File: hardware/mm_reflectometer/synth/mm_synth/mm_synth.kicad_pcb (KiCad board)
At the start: 6 copper layers, 680 parts, among them J1001 Conn_Coaxial, J1002 Conn_Coaxial, J1501 1725656, J1502 1053091202, J1601 USB_C_Receptacle_USB2.0, J1603 JTAG, J1604 Flash, J1701 Conn_Coaxial, J1702 Conn_Coaxial, J1801 SYZYGY-STD, J1802 PMOD, J1803 PMOD, J2001 Conn_Coaxial, J2002 Conn_Coaxial, J2003 Conn_Coaxial, J2004 Conn_Coaxial, J2101 USB_C_Receptacle_USB2.0, J301 Conn_Coaxial, J302 Conn_Coaxial, K301 1-1462051-1, Q1101 BC848W, Q1102 IRLML6401, Q1501 FDS6890A, Q1901 BC848W, Q1902 IRLML6401, Q2101 VBZA4435, Q301 IRLML6401, SW1601 SW_Push, SW1602 SW_Push, U1201 TLV9151IDCKR, U1301 LMT86DCK, U1302 TLV9151IDCKR, U1303 AD7298, U1304 VEMI65AB-HCI, U1501 LTM4622A, U1502 LTC4365DDB, U1503 LM3880MF-1AF, U1504 TLV70025_SOT353, U1505 TLV62569DRL, U1506 TLV62569DRL, U1507 TLV70018_SOT353, U1601 ECP5U_25_CABGA256, U1602 93LC56C, U1603 TPD3S014, U1604 FT2232HQ, U1605 W25Q32JVSS, U1701 IS66WVH16M8ALL, U1801 TLV62569DRL, U201 VEMI65AB-HCI, U202 LMX2820, U2101 HUSB238, U301 74AHC1G04, U302 DRV8837C, U303 LTC6957xMS-2, U401 MAAM-011101, U402 ADMV8416, U501 MAAM-011101, U502 XX1000-QT, U503 ADMV8432, U601 ADM7172ACPZ-5.0-R7, U602 LM3880MF-1AF, U603 LM27761, U604 TPS72301DB, U605 TPS72301DB, U606 ADP7158ACPZ-3.3-R7, U607 ADP7158ACPZ-3.3-R7, U608 LT3494, U701 ADRF5042, U702 VEMI65AB-HCI, U703 VEMI65AB-HCI, U704 ADRF5730, U705 MAAM-011109, U706 MAAM-011109, U707 FPC07181, U708 LTC5596, U801 LTC2636IDE-LZ10, U803 TLV9151IDCKR, U804 TLV9151IDCKR, U805 TLV9151IDCKR, U806 TLV9151IDCKR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

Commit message: commit mm_synth prior to updating from june to september kicad-nightly build
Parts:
- removed C631: 1 uF, Capacitor_SMD:C_0402_1005Metric
- added C719: 47 uF, Capacitor_Tantalum_SMD:CP_EIA-3528-15_AVX-H, F.Cu at (225.8, 39.2)
- added C720: 1 uF, Capacitor_SMD:C_0402_1005Metric, F.Cu at (244.8, 42.0)
- added R625: R_Small, Resistor_SMD:R_0402_1005Metric, F.Cu at (196.8, 43.1)
- added R626: R_Small, Resistor_SMD:R_0402_1005Metric, F.Cu at (186.9, 58.7)
- added R627: DNI, Resistor_SMD:R_0402_1005Metric, F.Cu at (183.5, 61.2)
- added R628: DNI, Resistor_SMD:R_0402_1005Metric, F.Cu at (188.8, 52.8)
- C1501, C1526: footprint Capacitor_SMD:CP_Elec_6.3x5.9 -> Capacitor_SMD:CP_Elec_10x12.5
- C1502, C1506: footprint Capacitor_SMD:C_0603_1608Metric -> Capacitor_SMD:C_0805_2012Metric
- C1503, C1509, C1512, C310: value 22 uF -> 10 uF
- C1507, C1508, C647, C648: footprint Capacitor_SMD:C_1210_3225Metric -> Capacitor_Tantalum_SMD:CP_EIA-3528-15_AVX-H
- C227: footprint Capacitor_SMD:C_0603_1608Metric -> Capacitor_SMD:C_1206_3216Metric
- C626, C628: value 1 uF -> DNI
- C630: value 1 uF -> 10 uF; footprint Capacitor_SMD:C_0402_1005Metric -> Capacitor_SMD:C_0805_2012Metric
- C633, C634: value 1 uF -> 1 nF
- U601: value ADM7172ACPZ-5.0-R7 -> ADM7171ACPZ-5.0-R7
- U606, U607: value ADP7158ACPZ-3.3-R7 -> ADM7171ACPZ-R7; footprint Package_DFN_QFN:DFN-10-1EP_3x3mm_P0.5mm_EP1.65x2.38mm -> Package_DFN_QFN:DFN-8-1EP_3x3mm_P0.5mm_EP1.66x2.38mm
- moved C642 152.5 mm to (209.5, 40.0)
- moved R608 151.1 mm to (207.3, 38.1)
- moved R623 147.8 mm to (189.5, 40.6)
- moved C603 146.0 mm to (194.0, 38.3)
- moved C613 145.6 mm to (193.3, 40.8)
- moved R606 145.0 mm to (201.5, 38.1)
- moved R612 144.5 mm to (203.7, 40.0)
- moved R615 143.9 mm to (197.7, 47.1)
- moved C601 143.9 mm to (185.3, 43.0)
- moved FB602 140.7 mm to (187.3, 45.5)
- moved R604 139.2 mm to (190.8, 50.1)
- moved C632 138.2 mm to (203.5, 44.5)
- moved C627 138.0 mm to (196.6, 51.5)
- moved R622 137.6 mm to (202.6, 42.6)
- moved C638 137.1 mm to (179.3, 49.9)
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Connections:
- net /rf_power/15V_BIAS_EN renamed /ctrl_power/DIGITAL_SEQ_EN
- C626 pad 2: GND -> Net-(C626-Pad2)
- C628 pad 2: GND -> Net-(C628-Pad2)
- C630 pad 1: Net-(C630-Pad1) -> +15V
- C636 pad 1: Net-(C636-Pad1) -> Net-(C626-Pad1)
- C637 pad 1: Net-(C637-Pad1) -> Net-(C628-Pad1)
- FB605 pad 1: Net-(C636-Pad1) -> Net-(C626-Pad1)
- FB606 pad 1: Net-(C637-Pad1) -> Net-(C628-Pad1)
- R621 pad 2: Net-(C636-Pad1) -> Net-(C626-Pad1)
- R622 pad 1: Net-(R622-Pad1) -> GND
- R622 pad 2: Net-(C637-Pad1) -> Net-(R621-Pad1)
- U606 pad 1: Net-(C636-Pad1) -> Net-(C626-Pad1)
- U606 pad 2: Net-(C636-Pad1) -> Net-(C626-Pad1)
- U606 pad 4: Net-(C626-Pad1) -> Net-(C633-Pad1)
- U606 pad 6: Net-(C633-Pad1) -> GND
- U606 pad 7: Net-(C633-Pad1) -> +4V
- U606 pad 8: Net-(C630-Pad1) -> +4V
- U606 pad 9: +4V -> GND
- U607 pad 1: Net-(C637-Pad1) -> Net-(C628-Pad1)
- U607 pad 2: Net-(C637-Pad1) -> Net-(C628-Pad1)
- U607 pad 3: Net-(R622-Pad1) -> Net-(R625-Pad1)
- U607 pad 4: Net-(C628-Pad1) -> Net-(C634-Pad1)
- U607 pad 6: Net-(C634-Pad1) -> GND
- U607 pad 7: Net-(C634-Pad1) -> +4V
- U607 pad 8: Net-(C631-Pad1) -> +4V
- U607 pad 9: +4V -> GND
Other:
- copper layers 6 -> 8
- board text added: "0"
- board text added: "0 mm"
- board text added: "0.0000 mm x 0.0000 mm"
- board text added: "0.0037"
- board text added: "0.01 mm"
- board text added: "0.02"
- board text added: "0.035 mm"
- board text added: "0.1 mm"
- board text added: "0.1270 mm / 0.1270 mm"
- board text added: "0.168 mm"
- board text added: "0.2032 mm"
- board text added: "0.35 mm"
- board text added: "1"
- board text added: "1.6360 mm"
- board text added: "3.3"
- board text added: "3.66"
- board text added: "3.7"
- board text added: "4"
- board text added: "8"
- board text added: "B.Cu"
- board text added: "B.Mask"
- board text added: "B.Paste"
- board text added: "B.Silkscreen"
- board text added: "BOARD CHARACTERISTICS"
- board text added: "Board Thickness:"
- board text added: "Board overall dimensions:"
- board text added: "Bottom Silk Screen"
- board text added: "Bottom Solder Mask"
- board text added: "Bottom Solder Paste"
- board text added: "Castellated pads:"
- board text added: "Color"
- board text added: "Copper Finish:"
- board text added: "Copper Layer Count:"
- board text added: "ENIG"
- board text added: "Epsilon R"
- board text added: "F.Cu"
- board text added: "F.Mask"
- board text added: "F.Paste"
- board text added: "F.Silkscreen"
- board text added: "FR4 (IPC 4101/126)"
- board text added: "Green"
- board text added: "Impedance Control:"
- board text added: "In1.Cu"
- board text added: "In2.Cu"
- board text added: "In3.Cu"
- board text added: "In4.Cu"
- board text added: "In5.Cu"
- board text added: "In6.Cu"
- board text added: "Layer Name"
- board text added: "Loss Tangent"
- board text added: "Material"
- board text added: "Min hole diameter:"
- board text added: "Min track/spacing:"
- board text added: "No"
- board text added: "Not specified"
- board text added: "Plated Board Edge:"
- board text added: "RO4350B"
- board text added: "Thickness (mm)"
- board text added: "Top Silk Screen"
- board text added: "Top Solder Mask"
- board text added: "Top Solder Paste"
- board text added: "Type"
- board text added: "White"
- board text added: "Yes"
- board text added: "copper"
- board text added: "core"
- board text added: "prepreg"

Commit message: component placement on mm synth
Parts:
- D1501: value RED -> PMEG030V050EPD; footprint LED_SMD:LED_0603_1608Metric -> Package_TO_SOT_SMD:Nexperia_CFP15_SOT-1289
- D1503: value PMEG030V050EPD -> RED; footprint Package_TO_SOT_SMD:Nexperia_CFP15_SOT-1289 -> LED_SMD:LED_0603_1608Metric
- moved L1502 364.9 mm to (402.8, 146.2)
- moved C1524 356.3 mm to (413.3, 168.0)
- moved C1525 356.0 mm to (413.3, 169.5)
- moved C1516 354.7 mm to (413.7, 174.0)
- moved C1517 353.5 mm to (413.7, 175.5)
- moved C1523 348.1 mm to (406.2, 149.2)
- moved U1503 345.8 mm to (410.6, 188.0)
- moved R1515 345.6 mm to (410.0, 190.5)
- moved L1501 345.3 mm to (396.9, 159.8)
- moved R1516 345.2 mm to (407.5, 187.5), turned to 90 degrees
- moved U1504 342.9 mm to (409.5, 175.5)
- moved R1518 338.8 mm to (405.5, 187.5), turned to 90 degrees
- moved U1506 337.2 mm to (399.2, 146.8)
- moved C1514 336.8 mm to (390.2, 159.2)
- moved C1513 334.9 mm to (405.7, 175.0)
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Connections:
- net /ctrl_power/DIGITAL_SEQ_EN renamed /rf_power/15V_BIAS_EN
- C1509 pad 1: Net-(C1509-Pad1) -> +9V
- D1501 pad 2: Net-(D1501-Pad2) -> Net-(D1501-Pad1)
- D1502 pad 3: +9V -> Net-(D1501-Pad3)
- D1503 pad 2: Net-(D1503-Pad1) -> Net-(D1503-Pad2)
- FB1501 pad 1: Net-(C1509-Pad1) -> VBUS
- FB1501 pad 2: Net-(D1503-Pad1) -> Net-(D1501-Pad1)
- FB1502 pad 1: VBUS -> VPP
- Q1501 pad 5: Net-(C1509-Pad1) -> +9V
- Q1501 pad 6: Net-(C1509-Pad1) -> +9V
- Q1501 pad 7: VPP -> Net-(D1501-Pad3)
- Q1501 pad 8: VPP -> Net-(D1501-Pad3)
- R1505 pad 2: VPP -> Net-(D1501-Pad3)
- R1510 pad 2: VPP -> Net-(D1501-Pad3)
- R1512 pad 2: Net-(D1501-Pad2) -> Net-(D1503-Pad2)
- U1502 pad 4: VPP -> Net-(D1501-Pad3)
- U1502 pad 6: Net-(C1509-Pad1) -> +9V
- U1502 pad 7: Net-(D1501-Pad1) -> Net-(D1503-Pad1)
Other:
- board text added: "Dielectric 1"
- board text added: "Dielectric 2"
- board text added: "Dielectric 3"
- board text added: "Dielectric 4"
- board text added: "Dielectric 5"
- board text added: "Dielectric 6"
- board text added: "Dielectric 7"
- board text added: "FR4 (IPC 4101/99)"
- board text removed: "0.0000 mm x 0.0000 mm"
- board text removed: "0.1270 mm / 0.1270 mm"
- board text removed: "0.2032 mm"
- board text removed: "1.6360 mm"
- board text removed: "3.7"
- board text removed: "8"
- board text removed: "BOARD CHARACTERISTICS"
- board text removed: "Board Thickness:"
- board text removed: "Board overall dimensions:"
- board text removed: "Castellated pads:"
- board text removed: "Copper Finish:"
- board text removed: "Copper Layer Count:"
- board text removed: "ENIG"
- board text removed: "FR4 (IPC 4101/126)"
- board text removed: "Impedance Control:"
- board text removed: "Min hole diameter:"
- board text removed: "Min track/spacing:"
- board text removed: "No"
- board text removed: "Plated Board Edge:"
- board text removed: "Yes"

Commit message: more component placement on mm synth
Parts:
- removed R1604: DNI, Resistor_SMD:R_0402_1005Metric
- added C1002: 10 nF, Capacitor_SMD:C_0402_1005Metric, F.Cu at (198.2, 117.2)
- added H2021: 2.5 mm, MountingHole:MountingHole_2.5mm_Pad_Via, F.Cu at (196.5, 140.8)
- added H2022: 2.5 mm, MountingHole:MountingHole_2.5mm_Pad_Via, F.Cu at (234.8, 135.0)
- added H2023: 2.5 mm, MountingHole:MountingHole_2.5mm_Pad_Via, F.Cu at (234.8, 103.2)
- added H2024: 2.5 mm, MountingHole:MountingHole_2.5mm_Pad_Via, F.Cu at (190.9, 243.5)
- added H2025: 2.5 mm, MountingHole:MountingHole_2.5mm_Pad_Via, F.Cu at (232.8, 207.2)
- added H2026: 2.5 mm, MountingHole:MountingHole_2.5mm_Pad_Via, F.Cu at (233.0, 243.5)
- added H2027: 2.5 mm, MountingHole:MountingHole_2.5mm_Pad_Via, F.Cu at (198.0, 150.0)
- added H2028: 2.5 mm, MountingHole:MountingHole_2.5mm_Pad_Via, F.Cu at (196.5, 108.5)
- added H2029: 2.5 mm, MountingHole:MountingHole_2.5mm_Pad_Via, F.Cu at (213.5, 59.2)
- added H2030: 2.5 mm, MountingHole:MountingHole_2.5mm_Pad_Via, F.Cu at (190.5, 207.2)
- added TP1601: TestPoint, TestPoint:TestPoint_Pad_D1.5mm, F.Cu at (-98.5, 126.5)
- C1803, C1804, C1806, C1807, C1808, C1809, C1810, C1811, C1812, C1813, C1814, L1801, R1802, R1803, R1804, R1805, R1806, R1807, R1808, R1809, R1810, R1811, R1812, R1813, R1814, R1815, R1816, R1817, R1818, R1819, R1820, R1821, R1822, R1823, R1824, U1801: moved to B.Cu
- J1001, J1002: footprint jtk_rf_footprints:sw_edge_oshpark_4layer -> vna_mm:SF2921-61345
- J301, J302: footprint jtk_rf_footprints:SMA_Cinch_142-0711-821_EdgeMount -> Connector_Coaxial:SMA_Amphenol_132134-16_Vertical
- moved C1509 425.3 mm to (-61.0, 191.3)
- moved C1512 425.3 mm to (-60.8, 186.5)
- moved C1526 425.3 mm to (-52.2, 190.8)
- moved D1503 425.3 mm to (-63.2, 193.0)
- moved Q1501 425.3 mm to (-63.8, 179.2)
- moved R1505 425.3 mm to (-70.2, 192.8)
- moved R1506 425.3 mm to (-70.2, 190.8)
- moved R1507 425.3 mm to (-70.2, 188.8)
- moved R1510 425.3 mm to (-68.5, 193.2)
- moved R1512 425.3 mm to (-63.2, 195.5)
- moved U1502 425.3 mm to (-66.8, 190.2)
- moved C1501 422.1 mm to (-95.5, 195.5)
- moved C1503 422.1 mm to (-89.0, 192.0)
- moved F1501 422.1 mm to (-105.9, 191.5)
- moved C1502 421.8 mm to (-57.7, 225.4)
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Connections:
- J1001 pad 1: /bypass/BYPASS_IN -> Net-(J1001-Pad1)
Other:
- board outline added: 170 x 105 mm
- board text added: "0.0000 mm x 0.0000 mm"
- board text added: "0.006"
- board text added: "0.0175 mm"
- board text added: "0.1270 mm / 0.1270 mm"
- board text added: "0.2 mm"
- board text added: "0.2032 mm"
- board text added: "0.3 mm"
- board text added: "1.5300 mm"
- board text added: "3.65"
- board text added: "8"
- board text added: "BOARD CHARACTERISTICS"
- board text added: "Board Thickness:"
- board text added: "Board overall dimensions:"
- board text added: "Castellated pads:"
- board text added: "Copper Finish:"
- board text added: "Copper Layer Count:"
- board text added: "ENIG"
- board text added: "Edge card connectors:"
- board text added: "IPC 4101/99"
- board text added: "Impedance Control:"
- board text added: "Isola I-Speed"
- board text added: "Min hole diameter:"
- board text added: "Min track/spacing:"
- board text added: "No"
- board text added: "Plated Board Edge:"
- board text added: "Yes"
- board text removed: "0.0037"
- board text removed: "0.168 mm"
- board text removed: "0.35 mm"
- board text removed: "3.66"
- board text removed: "FR4 (IPC 4101/99)"
- board text removed: "RO4350B"

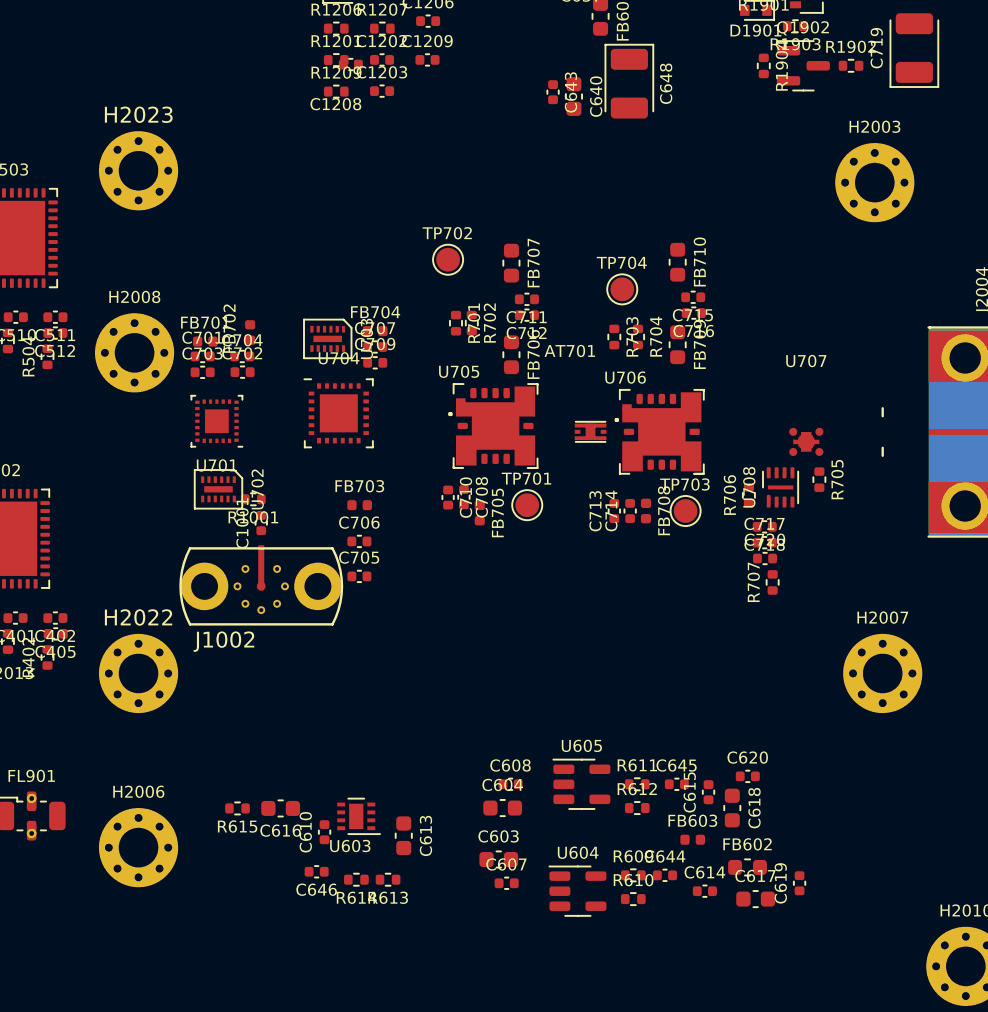
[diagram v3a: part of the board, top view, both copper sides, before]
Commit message: component placement
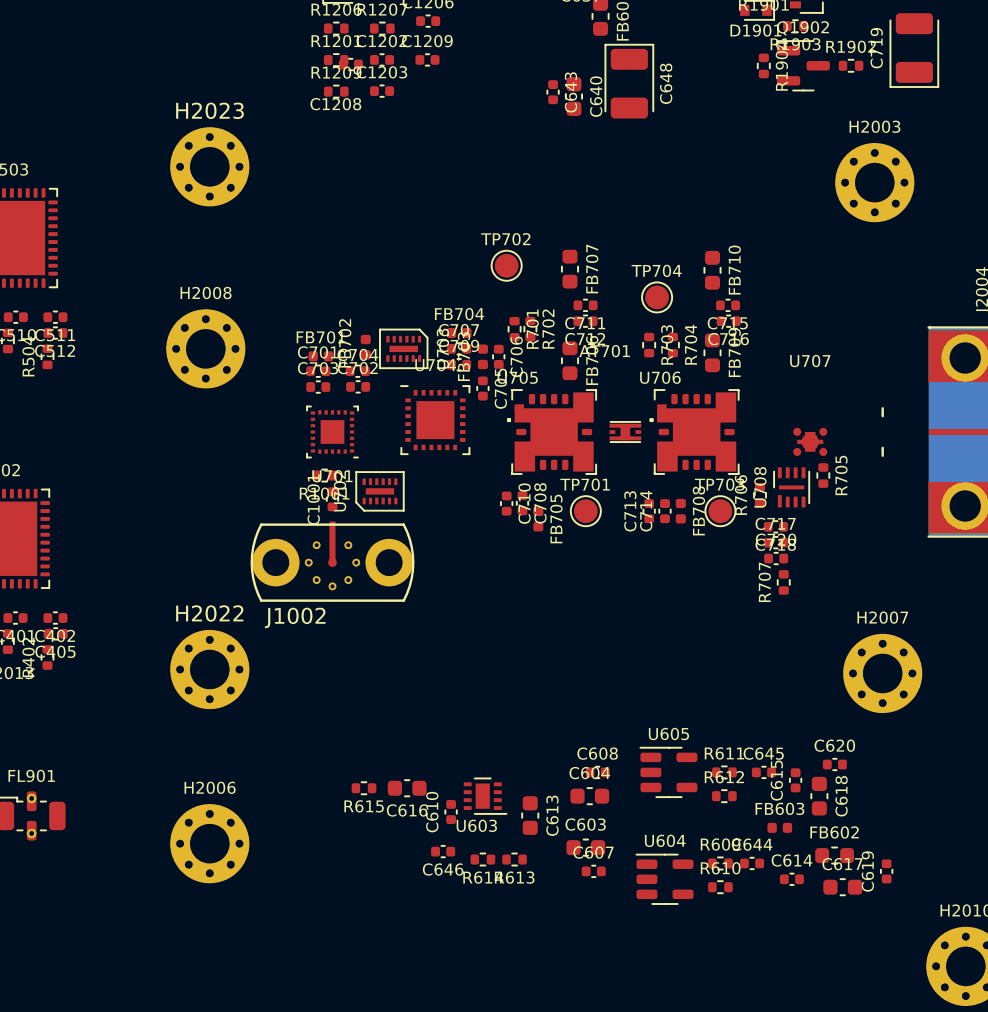
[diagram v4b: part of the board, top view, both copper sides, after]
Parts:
- moved C706 14.6 mm to (257.5, 115.0), turned to -90 degrees
- moved C705 14.2 mm to (256.5, 117.0), turned to -90 degrees
- moved FB703 12.2 mm to (256.5, 115.0), turned to 90 degrees
- moved U702 10.2 mm to (250.0, 123.5), turned to 0 degrees
- moved C610 8.09 mm to (254.5, 143.8)
- moved C613 8.09 mm to (259.5, 144.0)
- moved C616 8.09 mm to (251.7, 142.2)
- moved C646 8.09 mm to (254.0, 146.2)
- moved R613 8.09 mm to (258.5, 146.8)
- moved R614 8.09 mm to (256.5, 146.8)
- moved R615 8.09 mm to (249.0, 142.2)
- moved U603 8.09 mm to (256.5, 142.8)
- moved C702 7.36 mm to (248.6, 116.9)
- moved C701 7.36 mm to (246.1, 115.9)
- moved C703 7.36 mm to (246.1, 116.9)
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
